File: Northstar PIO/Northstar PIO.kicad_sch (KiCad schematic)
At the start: 32 parts, among them J1 Conn_01x02, J1A Configuration Header, J2 Conn_01x02, J3 Conn_01x02, J4 Conn_01x02, J5 Conn_01x02, J6 Conn_01x02, U1B 74LS74, U1C 74LS74, U1D SN74LS164N, U2A 74LS32, U2D 74LS03, U2D? 74LS175, U3A 74LS14, U3B 74LS37, U3C 74LS373, U3C? 74LS138, U3D 74LS373

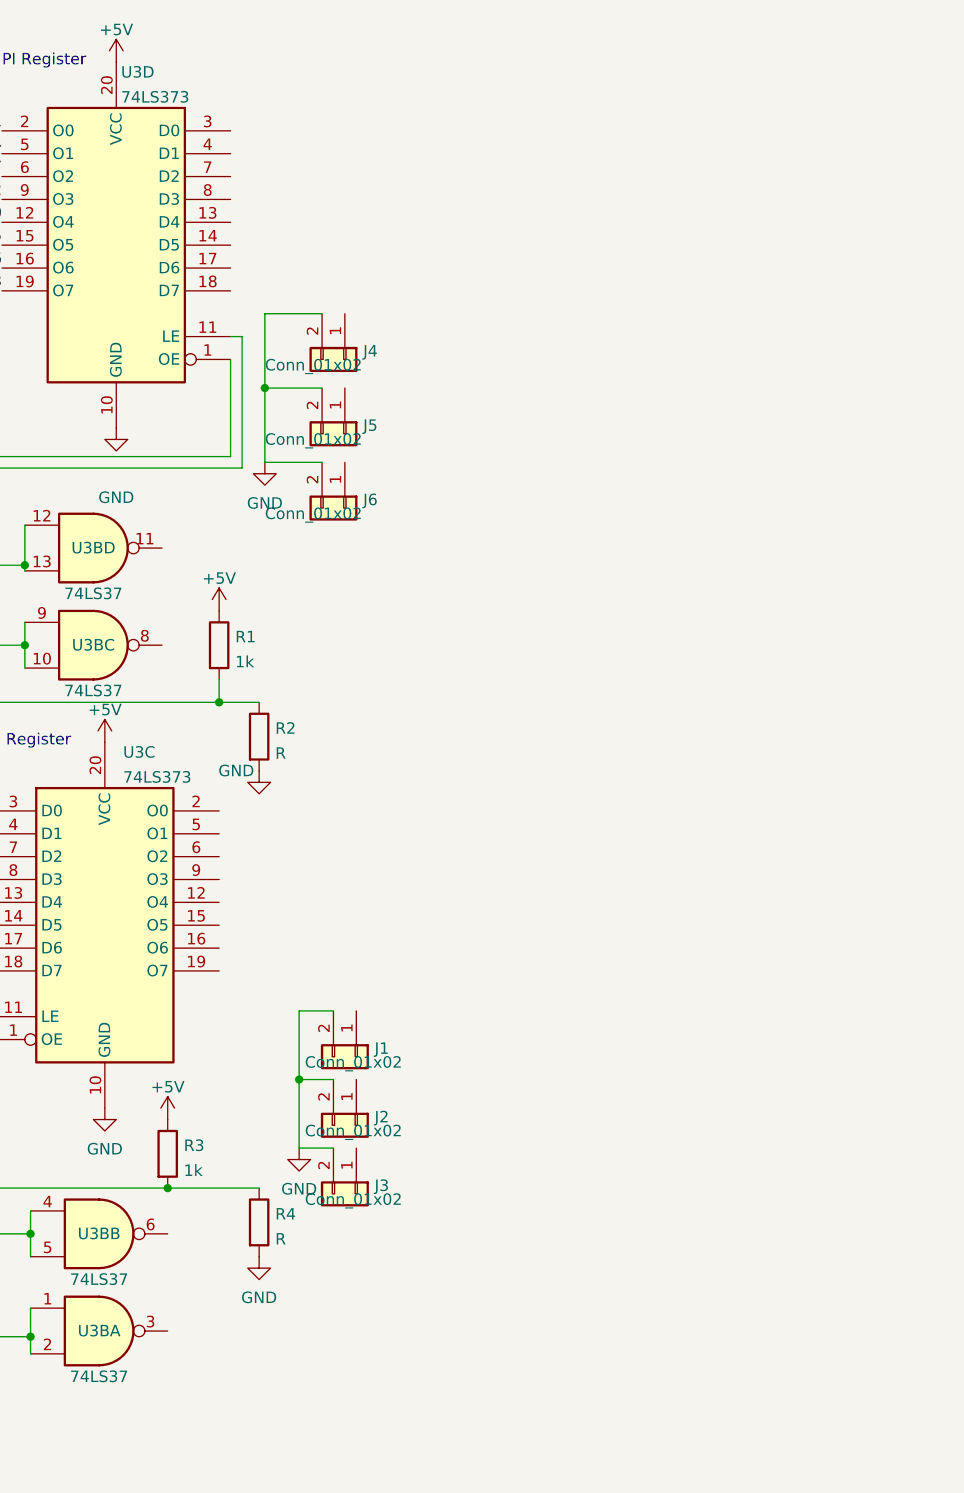
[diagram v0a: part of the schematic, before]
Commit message: finished PIO schematic (could use prettying up though)
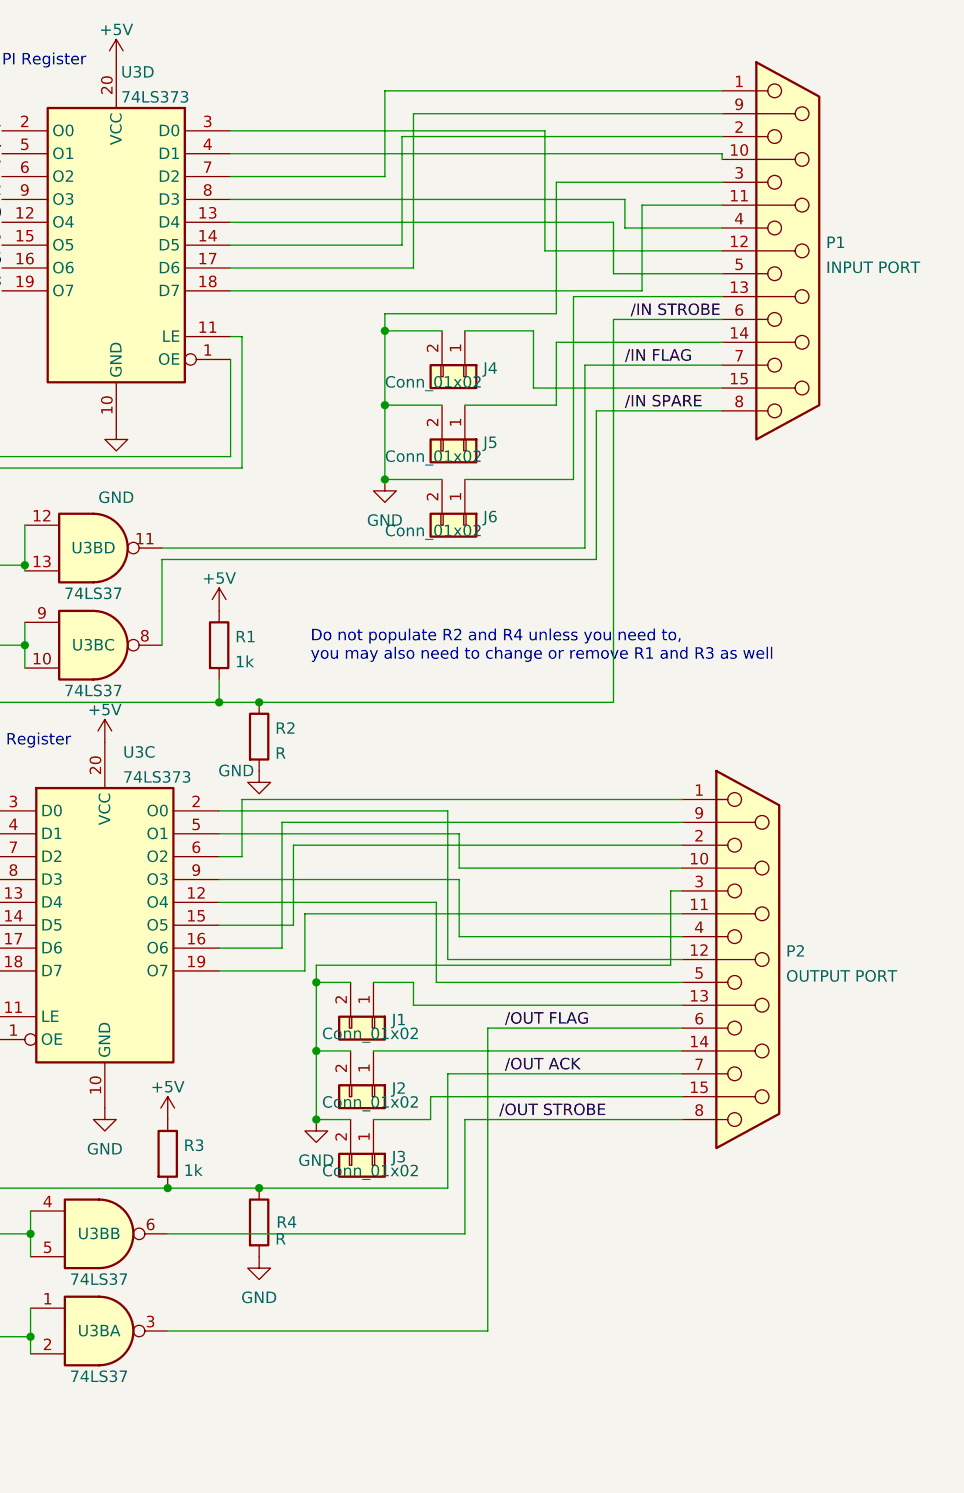
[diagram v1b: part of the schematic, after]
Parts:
- added P1: INPUT PORT, symbol Connector:DB15_Female
- added P2: OUTPUT PORT, symbol Connector:DB15_Female
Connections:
- net GND: now also P1.3, P2.3
- net /IN STROBE: now reaches R1.2, R2.1, U3A.13
- net /IN STROBE: now also P1.6
- net at J2.1 (Pin_1): now also P2.14 (P14)
- net at U3C.12 (O4): now also P2.5
- net at U3C.15 (O5): now also P2.2
- net at U3C.16 (O6): now also P2.9 (P9)
- net at U3C.19 (O7): now also P2.11 (P111)
- net at U3C.2 (O0): now also P2.12 (P12)
- net at U3C.5 (O1): now also P2.10 (P10)
- net at U3C.6 (O2): now also P2.1
- net at U3C.9 (O3): now also P2.4
- net at J1.1 (Pin_1): now also P2.13 (P13)
- net at U3D.13 (D4): now also P1.5
- net at U3D.14 (D5): now also P1.2
- net at U3D.17 (D6): now also P1.9 (P9)
- net at U3D.18 (D7): now also P1.11 (P111)
- net at U3D.3 (D0): now also P1.12 (P12)
- net at U3D.4 (D1): now also P1.10 (P10)
- net at U3D.7 (D2): now also P1.1
- net at U3D.8 (D3): now also P1.4
- net /IN SPARE: now reaches U3B.8
- net /IN SPARE: now also P1.8
- net at J4.1 (Pin_1): now also P1.15 (P15)
- net at J3.1 (Pin_1): now also P2.15 (P15)
- net /OUT ACK: now reaches R3.2, R4.1
- net /OUT ACK: now also P2.7
- net at J5.1 (Pin_1): now also P1.14 (P14)
- net /OUT FLAG: now reaches U3B.3
- net /OUT FLAG: now also P2.6
- net /OUT STROBE: now reaches U3B.6
- net /OUT STROBE: now also P2.8
- net /IN FLAG: now reaches U3B.11
- net /IN FLAG: now also P1.7
- net at J6.1 (Pin_1): now also P1.13 (P13)
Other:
- note added: "Do not populate R2 and R4 unless you need to, you may also need to change or remove R1 and R3 as well"
- moved on the sheet: J1, J2, J3, J4, J5, J6

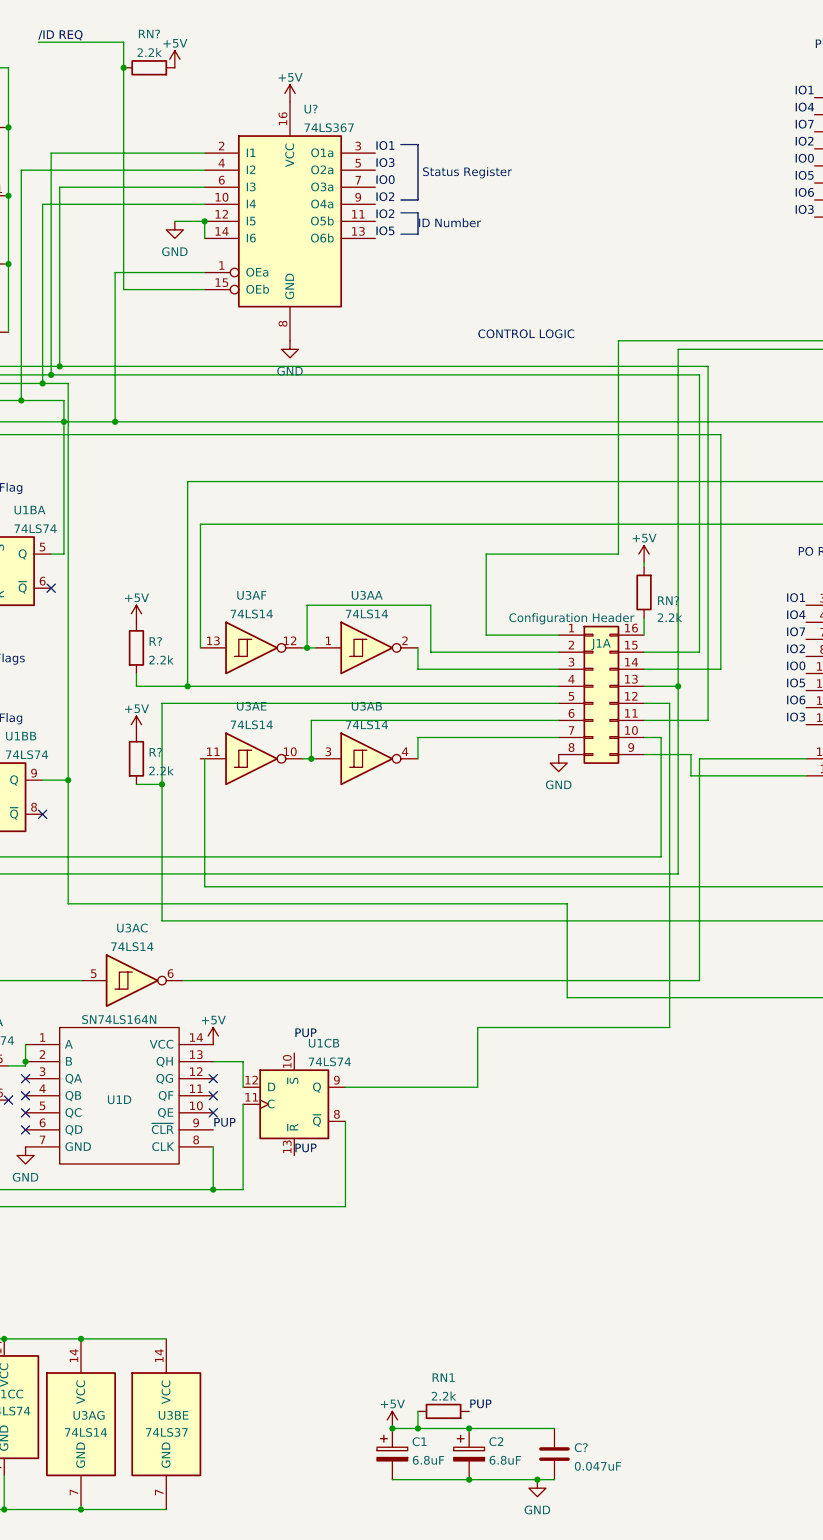
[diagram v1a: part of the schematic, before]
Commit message: made resistor network correct
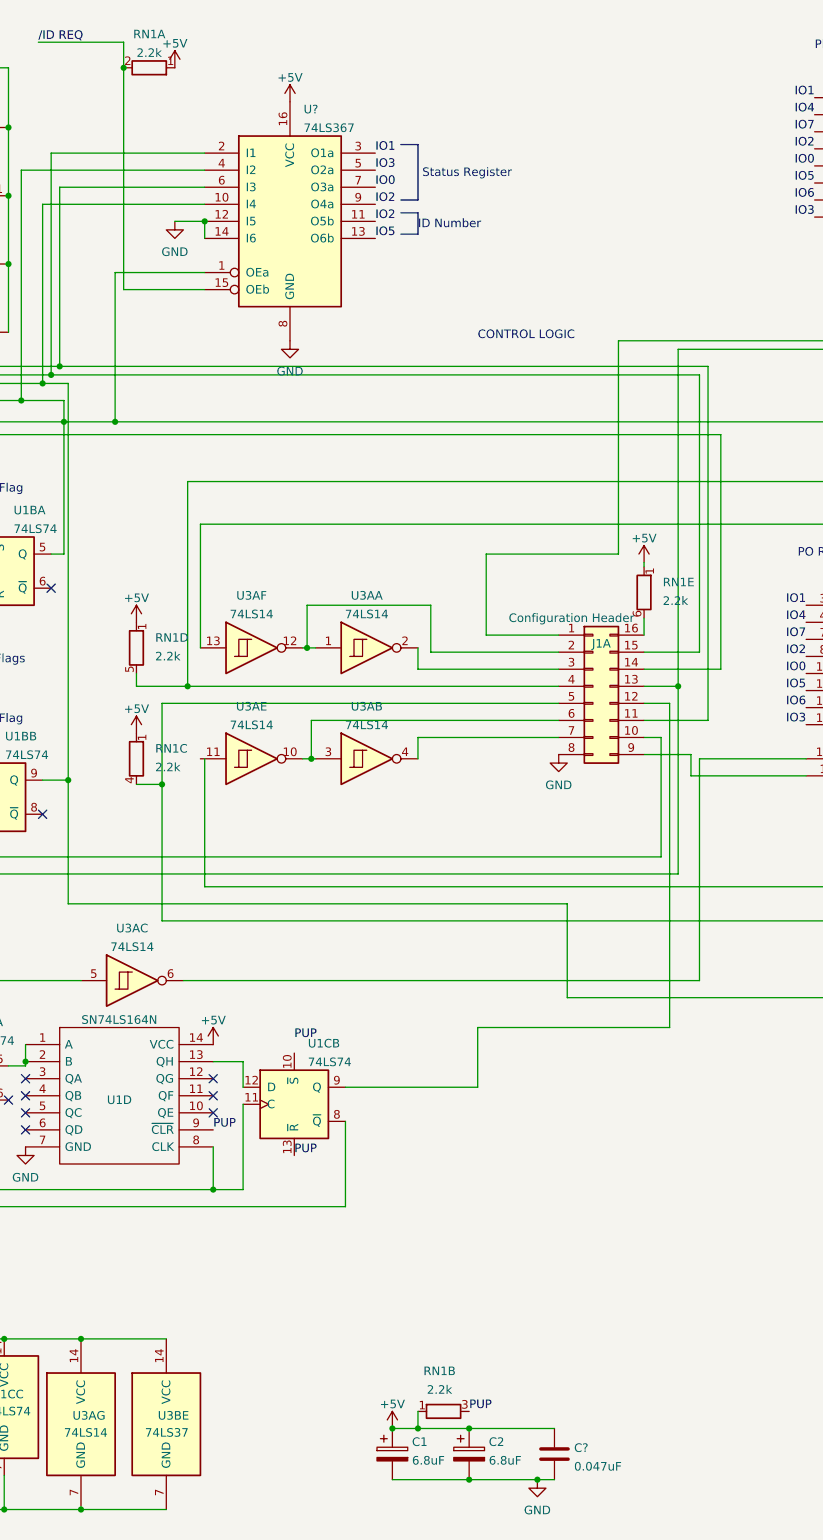
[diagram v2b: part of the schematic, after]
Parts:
- removed R? (x2): 2.2k, symbol Device:R
- removed RN1, RN? (x2): 2.2k, Resistor_THT:R_Axial_DIN0207_L6.3mm_D2.5mm_P15.24mm_Horizontal, symbol Device:R
- added RN1: 2.2k, Resistor_THT:R_Array_SIP6, symbol Device:R_Network05_Split
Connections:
- net +5V: now also RN1.1 (R1.1)
- net PUP: now also RN1.3 (R2.2)
- net /ID REQ: now also RN1.2 (R1.2)
- net at J1A.4 (Pin_4), U3B.10, U3B.9: now also RN1.5 (R4.2)
- net at J1A.16 (Pin_16): now also RN1.6 (R5.2)
- net at J1A.5 (Pin_5), U3B.4, U3B.5: now also RN1.4 (R3.2)

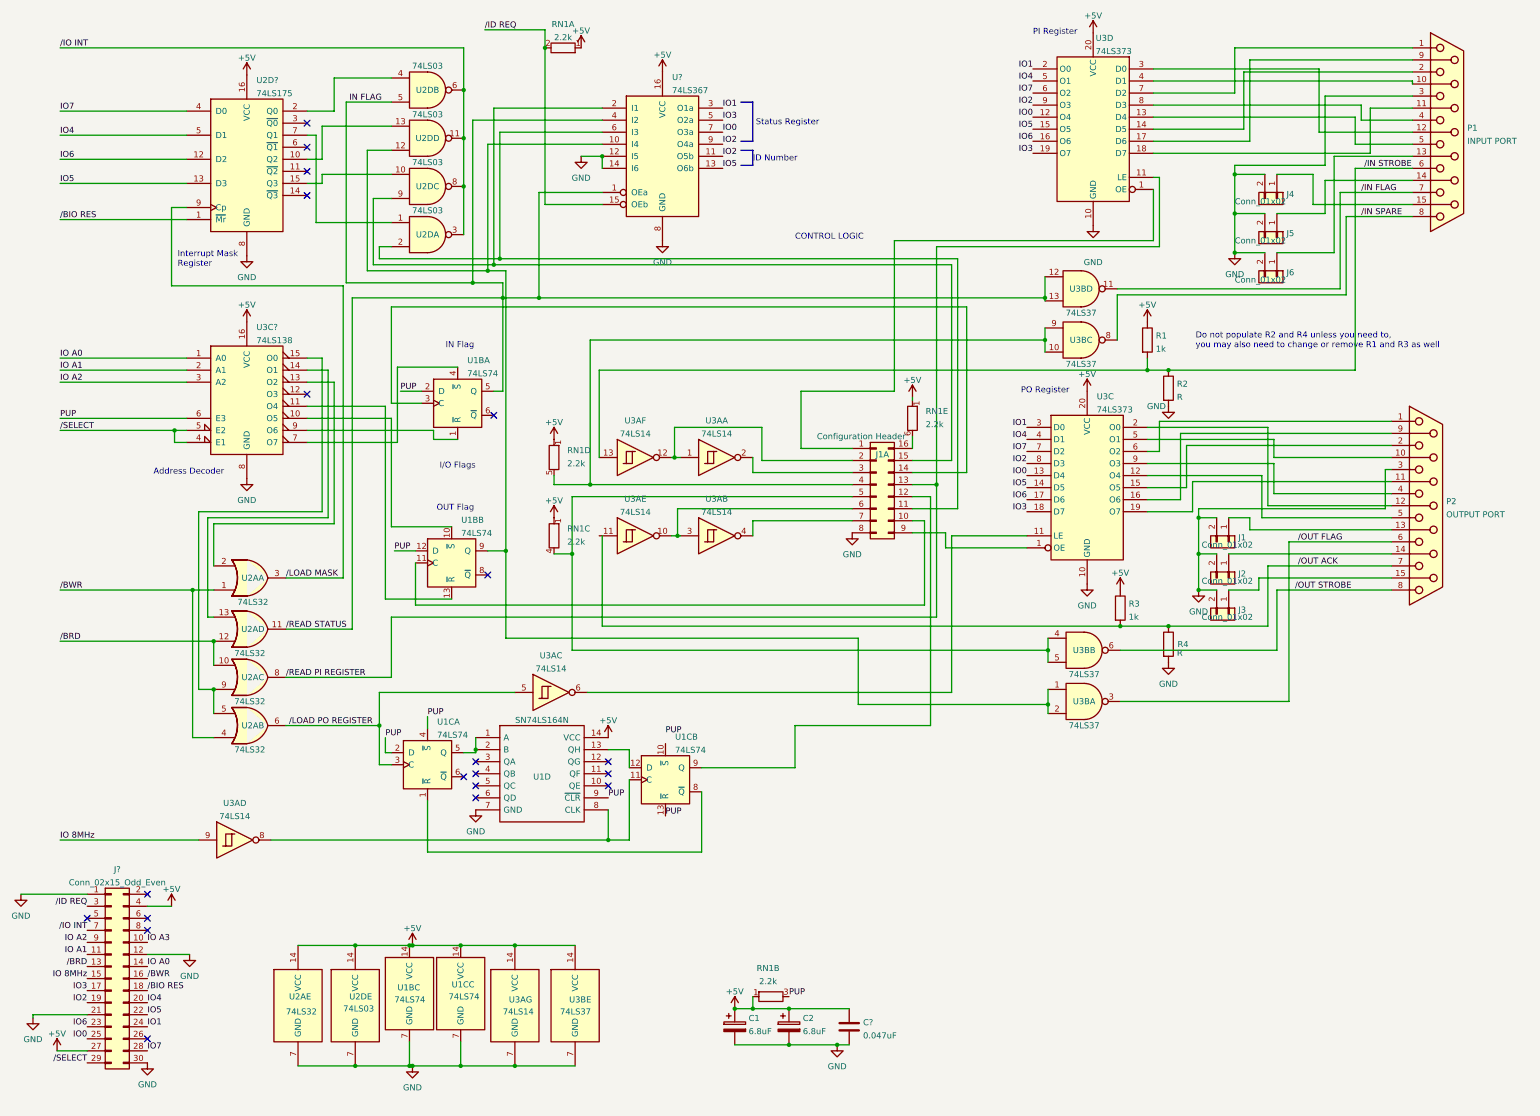
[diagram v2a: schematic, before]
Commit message: PIO first layout and silk done
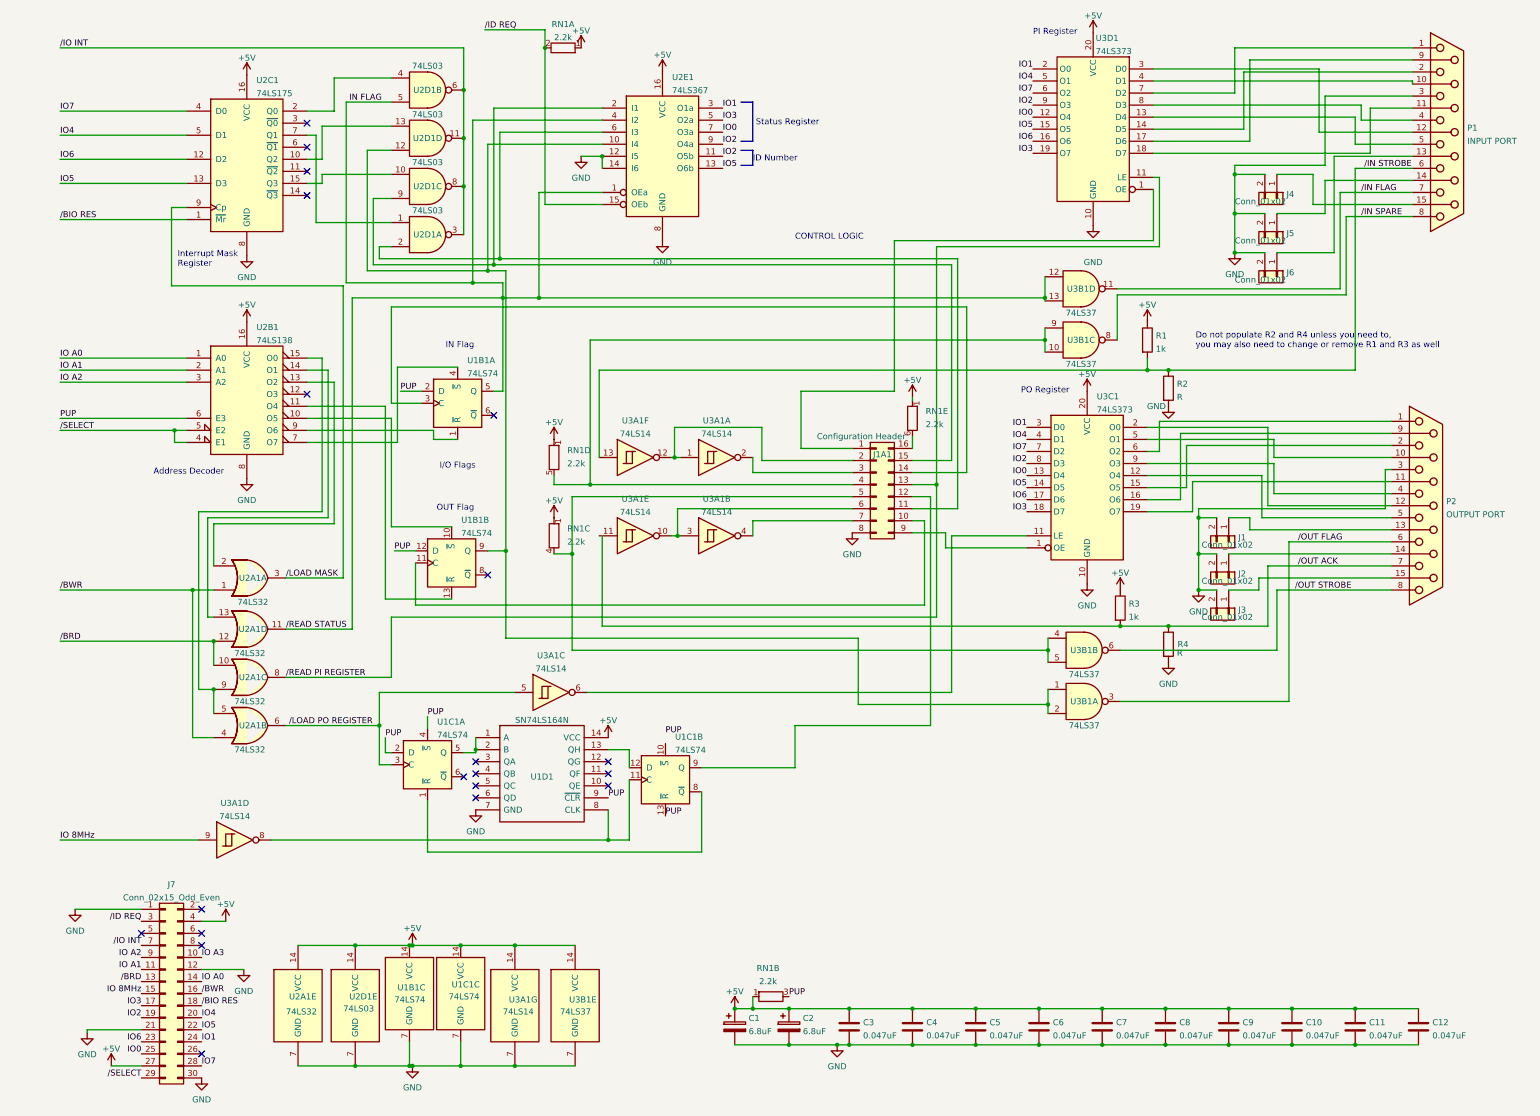
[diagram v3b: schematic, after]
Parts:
- added C10, C11, C12, C4, C5, C6, C7, C8, C9: 0.047uF, Capacitor_THT:C_Disc_D7.5mm_W2.5mm_P5.00mm, symbol Device:C
- J1, J2, J3, J4, J5, J6: footprint (none) -> Connector_PinHeader_2.54mm:PinHeader_1x02_P2.54mm_Vertical
- P1, P2: footprint (none) -> Connector_Dsub:DSUB-15_Female_Horizontal_P2.77x2.84mm_EdgePinOffset9.40mm
- R1, R2, R3, R4: footprint (none) -> Resistor_THT:R_Axial_DIN0207_L6.3mm_D2.5mm_P15.24mm_Horizontal
- U1B1: renamed from U1B; footprint (none) -> Package_DIP:DIP-14_W7.62mm
- U1C1: renamed from U1C; footprint (none) -> Package_DIP:DIP-14_W7.62mm
- U1D1: renamed from U1D; footprint DIP794W53P254L1930H508Q14N -> Package_DIP:DIP-14_W7.62mm
- U2A1: renamed from U2A; footprint (none) -> Package_DIP:DIP-14_W7.62mm
- U2E1: renamed from U?; footprint (none) -> Package_DIP:DIP-16_W7.62mm
- U3A1: renamed from U3A; footprint (none) -> Package_DIP:DIP-14_W7.62mm
- U3B1: renamed from U3B; footprint (none) -> Package_DIP:DIP-14_W7.62mm
- U3C1: renamed from U3C; footprint (none) -> Package_DIP:DIP-20_W7.62mm
- U3D1: renamed from U3D; footprint (none) -> Package_DIP:DIP-20_W7.62mm
- gave numbers to parts that had none: 4
- renumbered J1A to J1A1, U2D to U2D1
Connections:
- net +5V: now also C10.1, C11.1, C12.1, C4.1, C5.1, C6.1, C7.1, C8.1, C9.1
- net GND: now also C10.2, C11.2, C12.2, C4.2, C5.2, C6.2, C7.2, C8.2, C9.2
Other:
- moved on the sheet: J7
